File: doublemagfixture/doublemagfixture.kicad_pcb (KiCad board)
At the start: 2 copper layers, 90.2 x 74.3 mm, 32 parts, among them J1 Barrel_Jack_MountingPin, J2 Screw_Terminal_01x04, J3 Screw_Terminal_01x04, J4 Screw_Terminal_01x04, J5 Screw_Terminal_01x04, J6 Screw_Terminal_01x08, J7 Screw_Terminal_01x08, U1 easydriver_stepper_driver, U2 easydriver_stepper_driver, U3 easydriver_stepper_driver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

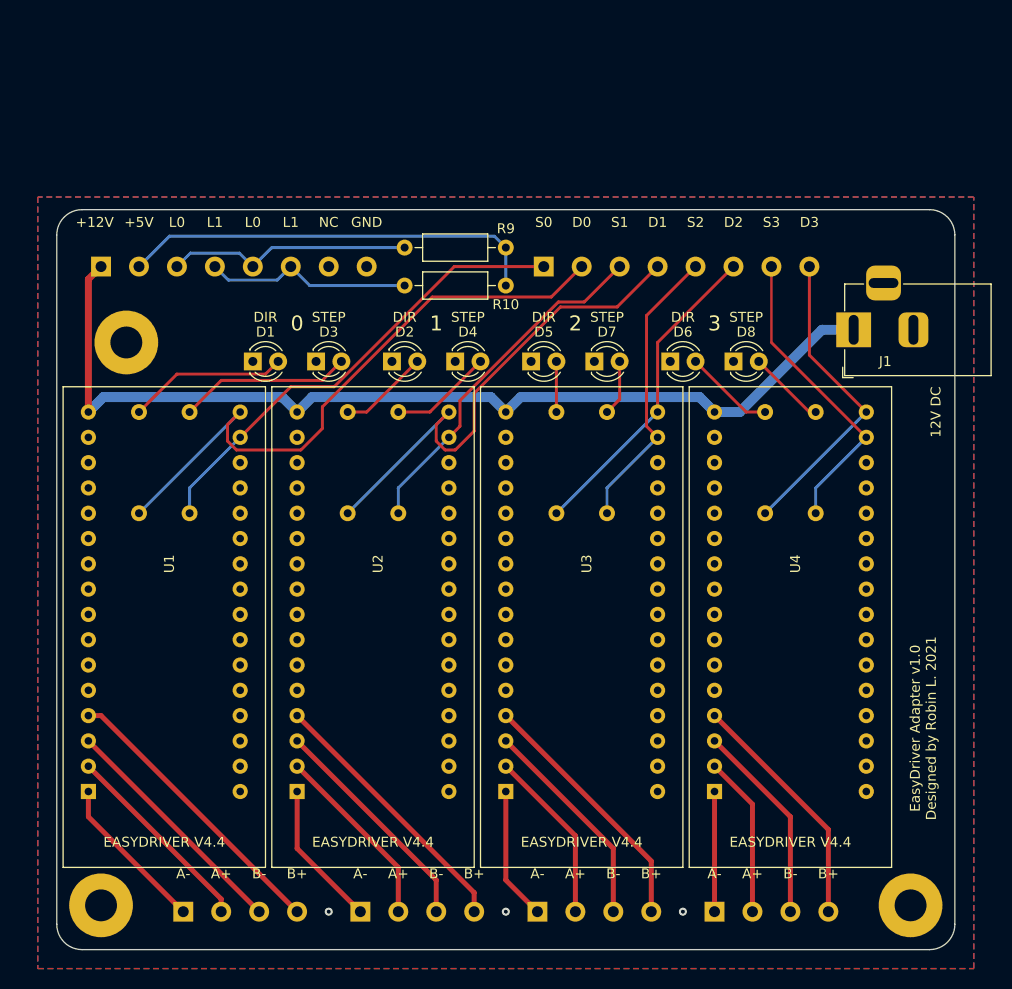
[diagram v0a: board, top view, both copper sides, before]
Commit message: change LED to 5mm
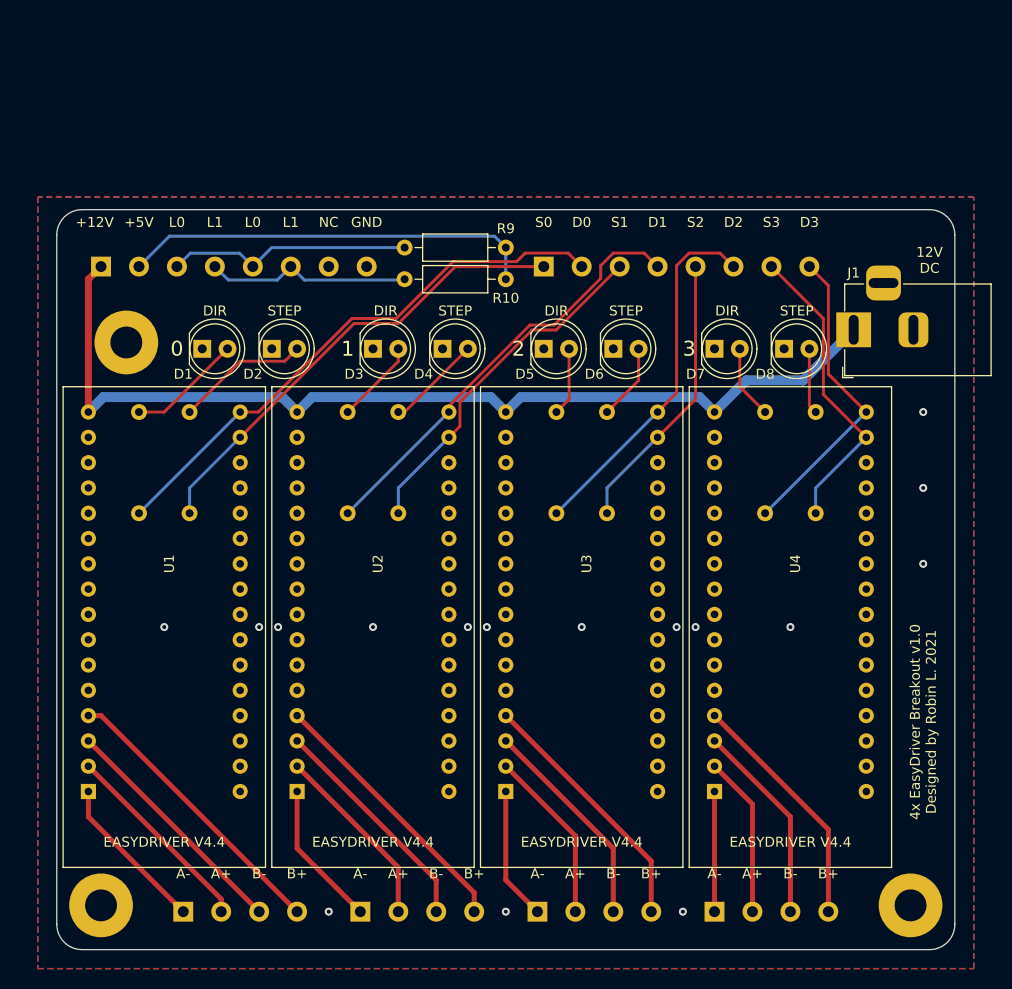
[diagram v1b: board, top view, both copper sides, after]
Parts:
- D1, D4, D5, D8: footprint LED_THT:LED_D3.0mm -> LED_THT:LED_D5.0mm
- D2: renamed from D3; footprint LED_THT:LED_D3.0mm -> LED_THT:LED_D5.0mm
- D3: renamed from D2; footprint LED_THT:LED_D3.0mm -> LED_THT:LED_D5.0mm
- D6: renamed from D7; footprint LED_THT:LED_D3.0mm -> LED_THT:LED_D5.0mm
- D7: renamed from D6; footprint LED_THT:LED_D3.0mm -> LED_THT:LED_D5.0mm
- moved D1 5.24 mm to (15.2, 14.6)
- moved D8 5.24 mm to (73.7, 14.6)
- moved D2 4.62 mm to (22.2, 14.6)
- moved D7 4.62 mm to (66.7, 14.6)
- moved D3 2.29 mm to (32.4, 14.6)
- moved D6 2.29 mm to (56.5, 14.6)
- moved D4 1.80 mm to (39.4, 14.6)
- moved D5 1.80 mm to (49.5, 14.6)
- moved R10 0.64 mm to (45.7, 7.62)
- renumbered J4 to J3, J3 to J4
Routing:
- net /dir0: track 62.6 -> 55.8 mm
- net /dir1: track 50.3 -> 43.6 mm
- net Net-(D1-Pad2): track 16.1 -> 11.5 mm
- net /dir2: track 32.1 -> 36.7 mm
- net Net-(D2-Pad2): track 17.3 -> 13.4 mm
- net Net-(D6-Pad2): track 5.61 -> 7.67 mm
- net Net-(D5-Pad2): track 5.08 -> 6.88 mm
- net Net-(D7-Pad2): track 9.09 -> 7.40 mm
- net Net-(D8-Pad2): track 7.82 -> 6.61 mm
- net /step2: track 29.4 -> 28.4 mm
- net Net-(D4-Pad2): track 10.4 -> 9.62 mm
- net +5V: track 42.4 -> 41.7 mm
- net Net-(D3-Pad2): track 9.09 -> 8.45 mm
- net GND: vias 3 -> 16
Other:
- rule pad_to_mask_clearance: 0.051 -> 0
- board text added: "4x EasyDriver Breakout v1.0 Designed by Robin L. 2021"
- board text removed: "EasyDriver Adapter v1.0 Designed by Robin L. 2021"

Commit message: add breakout board and reconfigure main board
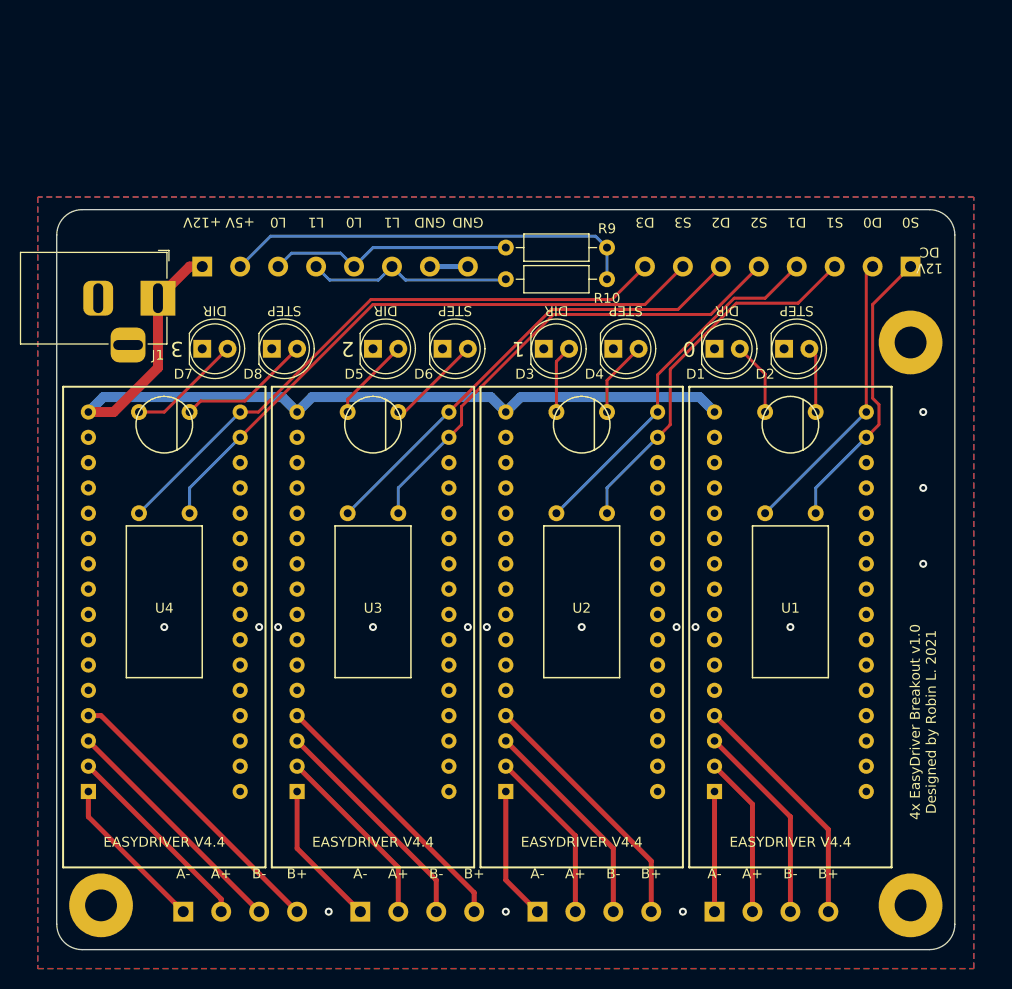
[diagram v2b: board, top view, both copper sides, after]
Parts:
- moved H1 78.7 mm to (86.4, 14.0)
- moved J1 69.9 mm to (10.8, 9.53), turned to 0 degrees
- moved U1 62.9 mm to (74.3, 36.2)
- moved U4 62.9 mm to (11.4, 36.2)
- moved R1 62.9 mm to (71.8, 21.0)
- moved R2 62.9 mm to (76.8, 21.0)
- moved R7 62.9 mm to (8.89, 21.0)
- moved R8 62.9 mm to (14.0, 21.0)
- moved J2 53.3 mm to (66.7, 71.1)
- moved J5 53.3 mm to (13.3, 71.1)
- moved D1 51.4 mm to (66.7, 14.6)
- moved D2 51.4 mm to (73.7, 14.6)
- moved D7 51.4 mm to (15.2, 14.6)
- moved D8 51.4 mm to (22.2, 14.6)
- moved J6 36.8 mm to (86.4, 6.35), turned to 180 degrees
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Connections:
- J7 pad 7: Net-(J7-Pad7) -> GND
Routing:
- net /step3: track 30.8 -> 61.3 mm
- net /dir3: track 31.3 -> 61.1 mm
- net /dir0: track 55.8 -> 29.2 mm
- net /step2: track 28.4 -> 49.0 mm
- net /step0: track 47.3 -> 29.2 mm
- net /dir2: track 36.7 -> 47.7 mm
- net +12V: track 99.1 -> 88.2 mm
- net /dir1: track 43.6 -> 36.6 mm
- net Net-(D2-Pad2): track 13.4 -> 6.61 mm
- net Net-(D8-Pad2): track 6.61 -> 13.4 mm
- net Net-(J5-Pad4): track 24.4 -> 29.1 mm
- net Net-(J2-Pad4): track 29.1 -> 24.4 mm
- net Net-(D7-Pad2): track 7.40 -> 11.5 mm
- net Net-(D1-Pad2): track 11.5 -> 7.40 mm
- net Net-(J5-Pad2): track 16.2 -> 20.1 mm
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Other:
- board text removed: "NC"

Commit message: add 3D mag work
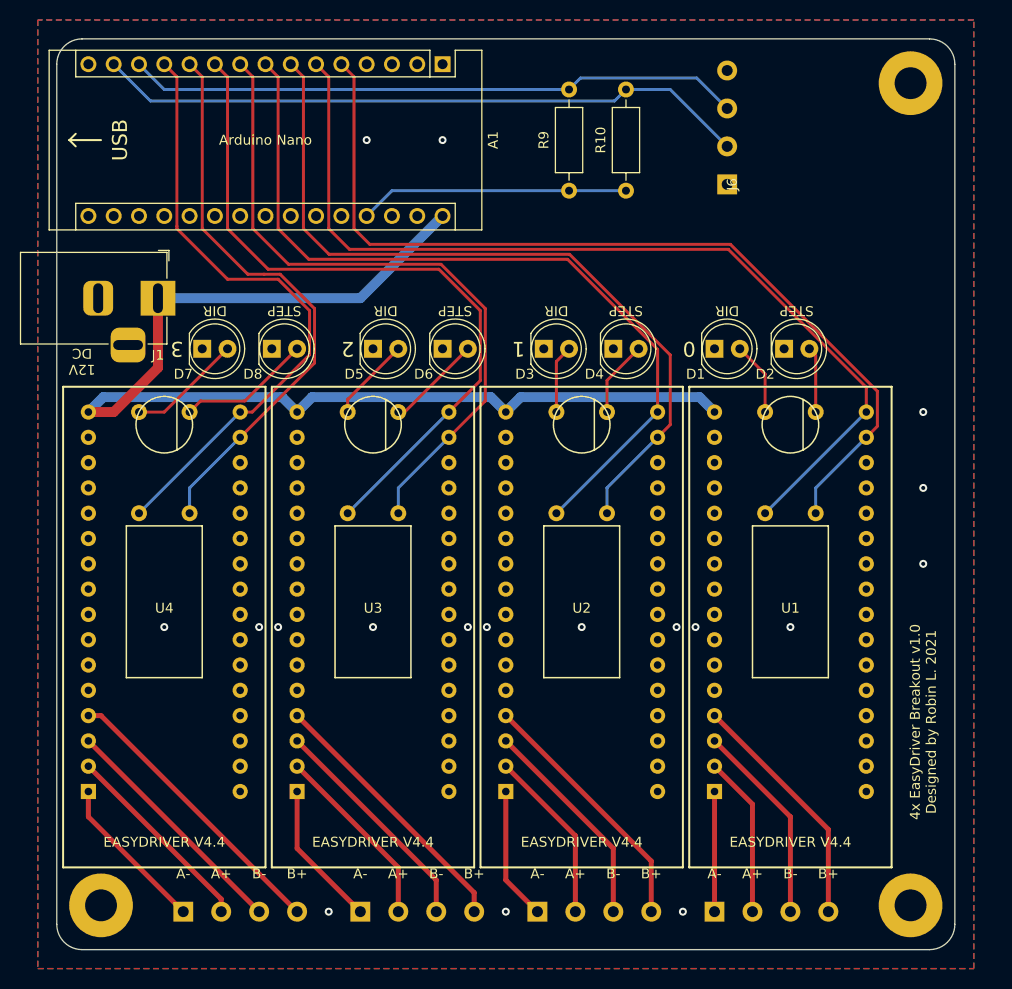
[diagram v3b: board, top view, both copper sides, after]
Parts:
- removed J7: Screw_Terminal_01x08, doublemag:CONN_1x8_3.81mm
- added A1: Arduino_Nano_v3.x, Module:Arduino_Nano, F.Cu at (39.4, -14.0)
- J6: value Screw_Terminal_01x08 -> Screw_Terminal_01x04; footprint doublemag:CONN_1x8_3.81mm -> doublemag:CONN_1x4_3.81mm
- moved H1 26.0 mm to (86.4, -12.1)
- moved J6 20.2 mm to (67.9, -1.91), turned to 90 degrees
- moved R10 9.09 mm to (57.8, -1.27), turned to 90 degrees
- moved R9 6.87 mm to (52.1, -1.27), turned to 90 degrees
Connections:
- J6 pad 1: /step0 -> GND
- J6 pad 2: /dir0 -> /lim1
- J6 pad 3: /step1 -> /lim0
- J6 pad 4: /dir1 -> Net-(J6-Pad4)
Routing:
- net /dir0: track 29.2 -> 94.5 mm
- net /step0: track 29.2 -> 91.2 mm
- net /lim1: track 20.8 -> 66.0 mm
- net /dir1: track 36.6 -> 80.8 mm
- net /step1: track 37.9 -> 77.6 mm
- net /lim0: track 24.8 -> 61.8 mm
- net +12V: track 88.2 -> 114.4 mm
- net /dir2: track 47.7 -> 71.7 mm
- net /step2: track 49.0 -> 67.9 mm
- net +5V: track 41.7 -> 27.1 mm
- net /step3: track 61.3 -> 57.4 mm
- net GND: track 3.81 -> 0.00 mm, vias 16 -> 18
- net /dir3: track 61.1 -> 61.9 mm
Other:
- board size 90.2 x 74.3 mm -> 90.2 x 91.4 mm
- board text added: "Arduino Nano"
- board text added: "USB"
- board text removed: "+12V"
- board text removed: "+5V"
- board text removed: "D0"
- board text removed: "D1"
- board text removed: "D2"
- board text removed: "D3"
- board text removed: "GND"
- board text removed: "L0"
- board text removed: "L1"
- board text removed: "S0"
- board text removed: "S1"
- board text removed: "S2"
- board text removed: "S3"
